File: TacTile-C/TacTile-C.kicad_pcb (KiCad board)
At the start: 2 copper layers, 59.9 x 59.9 mm, 45 parts, among them J1 Conn_01x02, J10 Conn_01x02, J11 Conn_01x02, J12 Conn_01x02, J13 Conn_01x02, J14 Conn_01x02, J15 Conn_01x02, J16 Conn_01x02, J17 Conn_01x02, J18 Conn_01x04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

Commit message: Mounted ICs without sockets to save space
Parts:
- U1: footprint Package_DIP:DIP-6_W7.62mm_Socket -> Package_DIP:DIP-6_W7.62mm
- U2, U3, U4, U5, U6, U7, U8: footprint Package_DIP:DIP-16_W7.62mm_Socket -> Package_DIP:DIP-16_W7.62mm

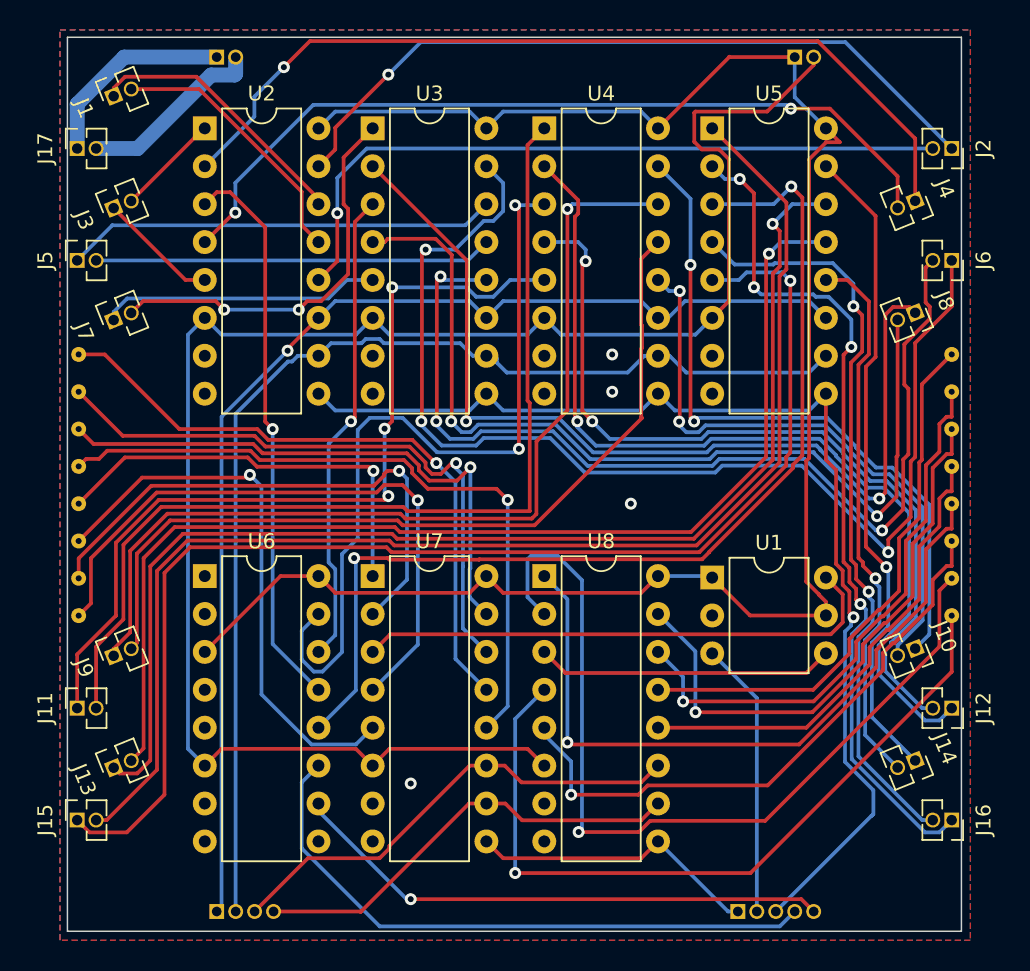
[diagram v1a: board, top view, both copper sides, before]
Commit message: Added photoresistor footprint and enlarged main boards to 60mm
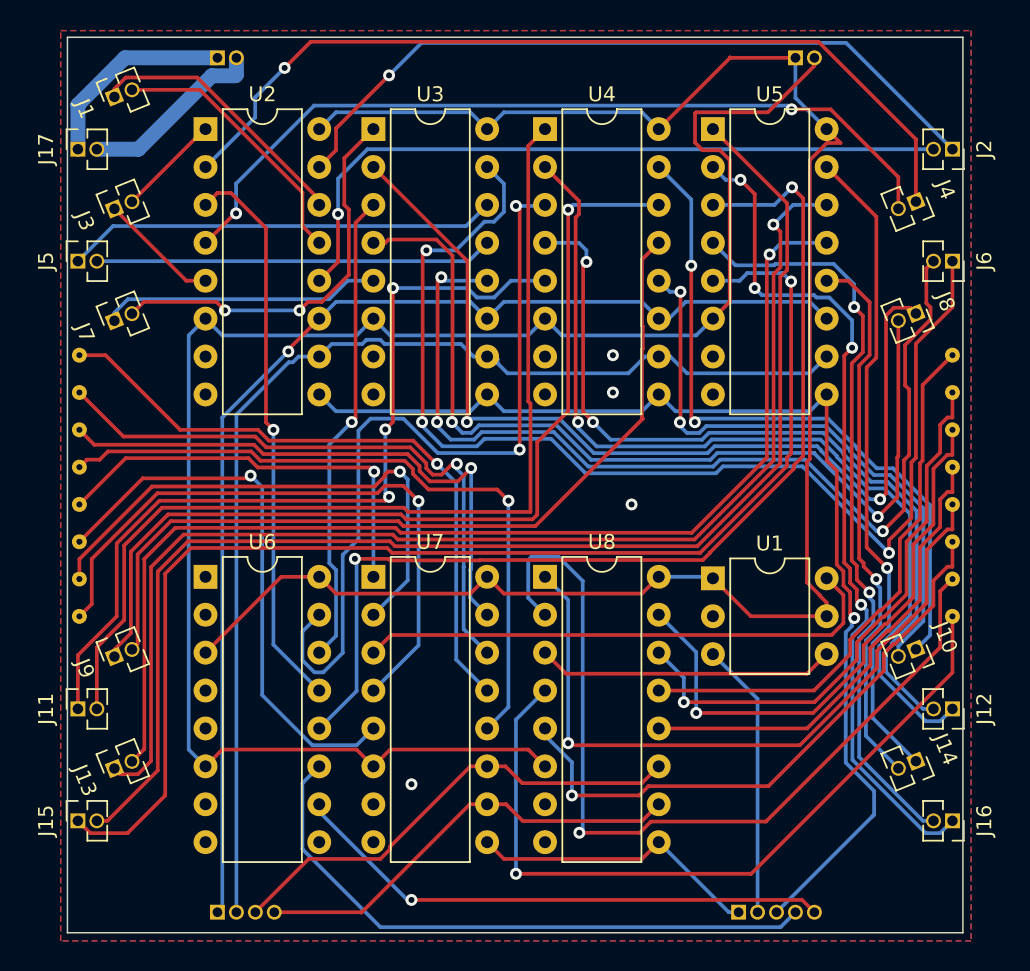
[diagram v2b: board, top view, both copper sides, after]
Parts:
- moved J4 0.07 mm to (81.9, 36.0)
- moved J8 0.07 mm to (81.9, 43.5)
- moved J1 0.07 mm to (28.1, 29.0)
- moved J11 0.07 mm to (25.7, 70.0)
- moved J13 0.07 mm to (28.1, 74.0)
- moved J15 0.07 mm to (25.7, 77.5)
- moved J17 0.07 mm to (25.7, 32.5)
- moved J20 0.07 mm to (35.0, 26.4)
- moved J21 0.07 mm to (73.8, 26.4)
- moved J3 0.07 mm to (28.1, 36.5)
- moved J5 0.07 mm to (25.7, 40.0)
- moved J7 0.07 mm to (28.1, 44.0)
- moved J9 0.07 mm to (28.1, 66.5)
- moved JMP1 0.07 mm to (25.8, 46.3)
- moved JMP2 0.07 mm to (25.8, 48.8)
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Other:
- board size 59.9 x 59.9 mm -> 60 x 60 mm

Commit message: Enlarged B-C interface to 2.54 pitch connectors
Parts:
- J18: footprint Connector_PinHeader_1.27mm:PinHeader_1x04_P1.27mm_Vertical -> Connector_PinHeader_2.54mm:PinHeader_1x04_P2.54mm_Vertical
- J19: footprint Connector_PinHeader_1.27mm:PinHeader_1x05_P1.27mm_Vertical -> Connector_PinHeader_2.54mm:PinHeader_1x05_P2.54mm_Vertical
- J20, J21: footprint Connector_PinHeader_1.27mm:PinHeader_1x02_P1.27mm_Vertical -> Connector_PinHeader_2.54mm:PinHeader_1x02_P2.54mm_Vertical
- moved J19 5.13 mm to (64.8, 83.6)
- moved J21 1.32 mm to (72.5, 26.4)
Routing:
- net /LS7: track 41.6 -> 35.9 mm
- net /LS3: track 29.7 -> 25.9 mm
- net /LS2: track 32.1 -> 29.5 mm
- net /LS4: track 19.7 -> 17.2 mm
- net /GND: track 12.5 -> 13.4 mm
- net /LS5: track 18.5 -> 17.7 mm
- net /VCC: track 123.3 -> 122.5 mm
- net /LS1: track 77.5 -> 76.8 mm
- net /LS6: track 76.0 -> 75.5 mm

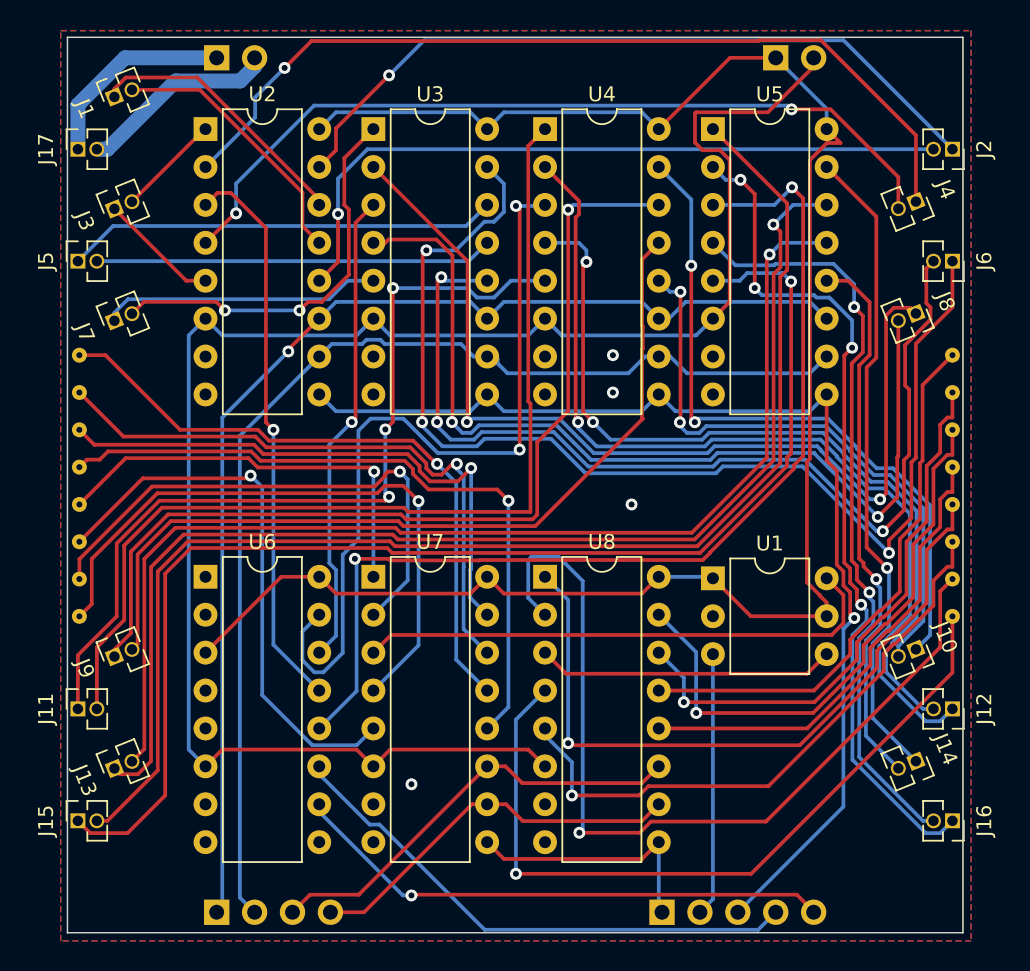
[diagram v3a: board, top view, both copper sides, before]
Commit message: Finished enlarging pins on C, D, L1, L2
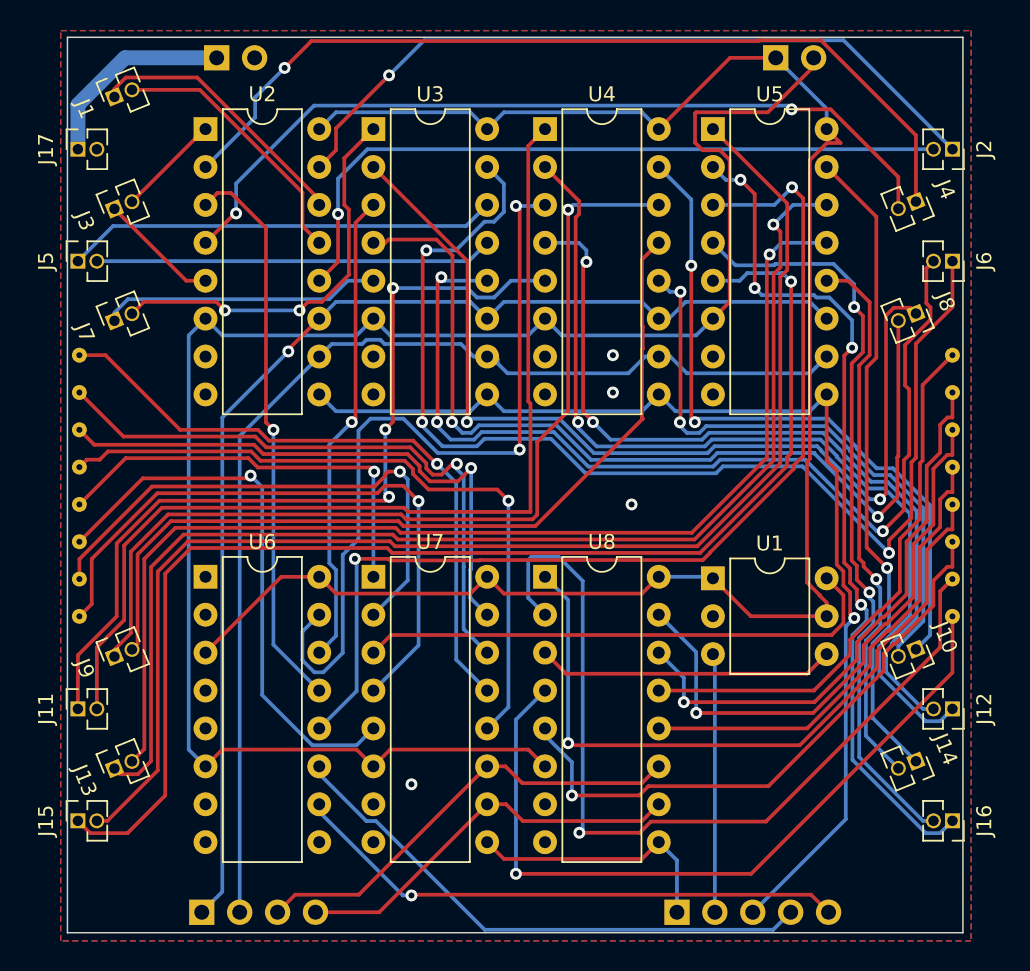
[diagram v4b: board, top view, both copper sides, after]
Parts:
- moved J18 1.00 mm to (34.0, 83.6)
- moved J19 1.00 mm to (65.8, 83.6)
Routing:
- net /GND: track 13.4 -> 0.00 mm
- net /LS3: track 25.9 -> 26.9 mm
- net /LS2: track 29.5 -> 30.5 mm
- net /LS7: track 35.9 -> 36.9 mm
- net /LS8: track 36.5 -> 37.5 mm

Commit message: Used 16DIP demultiplexer instead of single demultiplexer
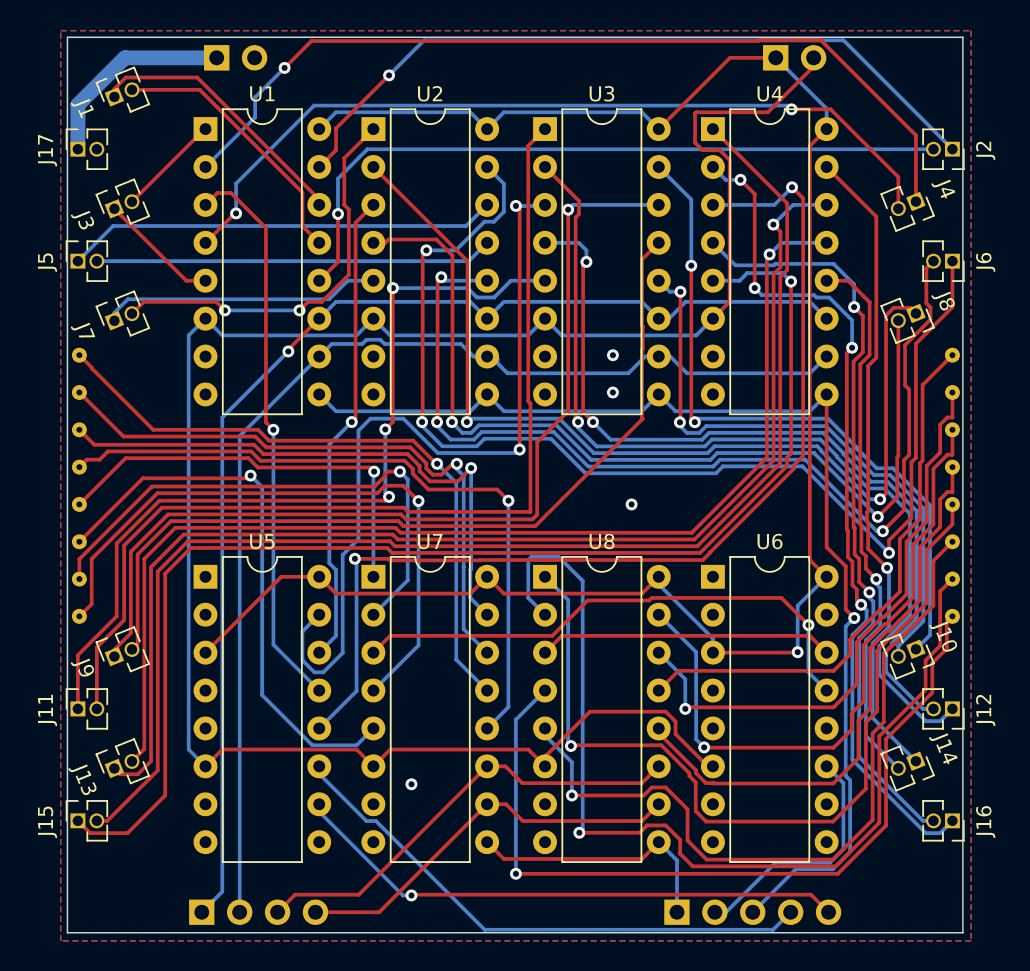
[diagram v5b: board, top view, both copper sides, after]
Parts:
- removed the U1 at (68.2, 61.2)
- added U6: 74HC4051, Package_DIP:DIP-16_W7.62mm, F.Cu at (68.2, 61.1)
- renumbered U2 to U1, U3 to U2, U4 to U3, U5 to U4, U6 to U5
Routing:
- net /LEN: track 118.0 -> 133.2 mm
- net /INP45: track 40.4 -> 50.9 mm
- net /INP44: track 48.0 -> 57.6 mm
- net /INP46: track 59.8 -> 67.1 mm
- net /INP43: track 31.8 -> 38.3 mm
- net /INP42: track 38.6 -> 43.7 mm
- net /INP47: track 51.7 -> 55.1 mm
- net /LS6: track 75.1 -> 76.8 mm
- net /INP41: track 37.6 -> 39.1 mm
- net /VCC: track 122.5 -> 123.8 mm, vias 0 -> 1
- net /LS5: track 17.3 -> 16.4 mm
- net Net-(U6-A0): track 35.8 -> 36.3 mm, vias 0 -> 1

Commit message: Redid A board with MOSFETs sinking current
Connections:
- net /INP0 renamed /B0
- net /INP1 renamed /B1
- net /INP10 renamed /B10
- net /INP11 renamed /B11
- net /INP12 renamed /B12
- net /INP13 renamed /B13
- net /INP14 renamed /B14
- net /INP15 renamed /B15
- net /INP16 renamed /B16
- net /INP17 renamed /B17
- net /INP18 renamed /B18
- net /INP19 renamed /B19
- net /INP2 renamed /B2
- net /INP20 renamed /B20
- net /INP21 renamed /B21
- net /INP22 renamed /B22
- net /INP23 renamed /B23
- net /INP24 renamed /B24
- net /INP25 renamed /B25
- net /INP26 renamed /B26
- net /INP27 renamed /B27
- net /INP28 renamed /B28
- net /INP29 renamed /B29
- net /INP3 renamed /B3
- net /INP30 renamed /B30
- net /INP31 renamed /B31
- net /INP32 renamed /A0
- net /INP33 renamed /A1
- net /INP34 renamed /A2
- net /INP35 renamed /A3
- net /INP36 renamed /A4
- net /INP37 renamed /A5
- net /INP38 renamed /A6
- net /INP39 renamed /A7
- net /INP4 renamed /B4
- net /INP40 renamed /A8
- net /INP41 renamed /A9
- net /INP42 renamed /A10
- net /INP43 renamed /A11
- net /INP44 renamed /A12
- net /INP45 renamed /A13
- net /INP46 renamed /A14
- net /INP47 renamed /A15
- net /INP5 renamed /B5
- net /INP6 renamed /B6
- net /INP7 renamed /B7
- net /INP8 renamed /B8
- net /INP9 renamed /B9

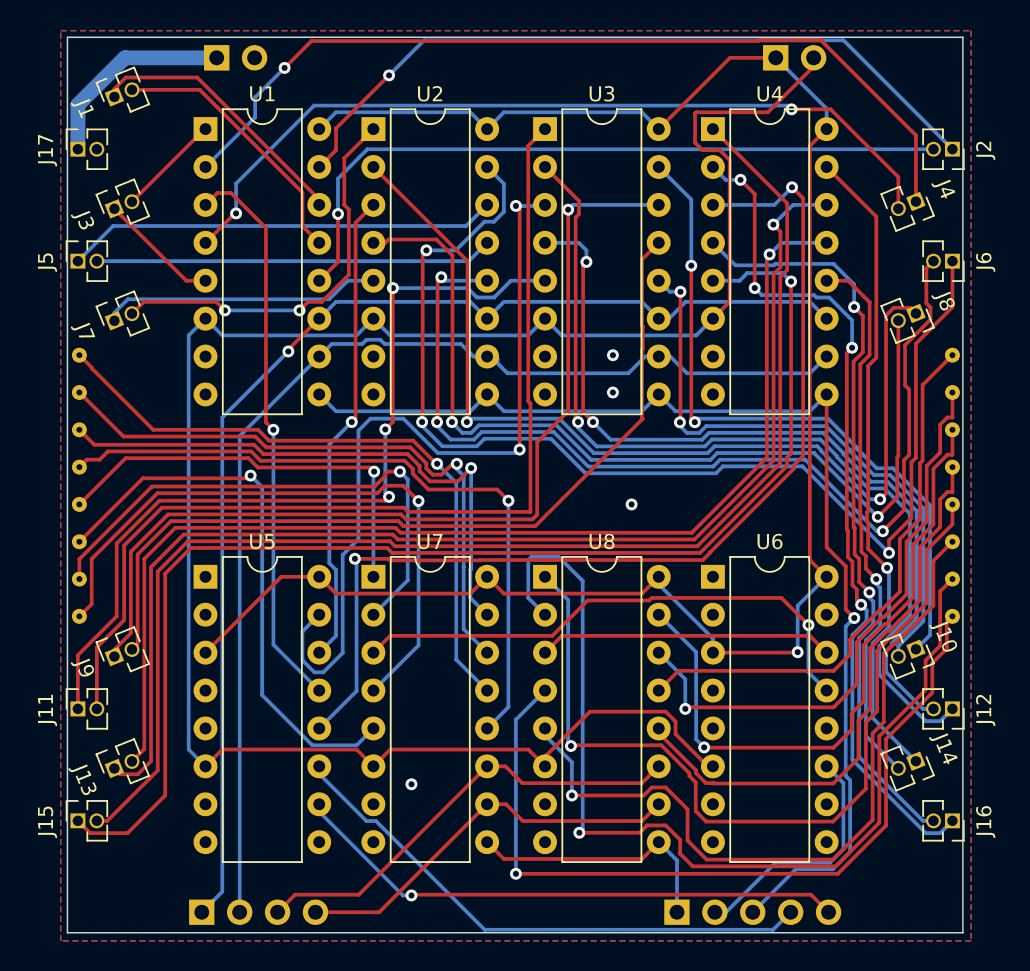
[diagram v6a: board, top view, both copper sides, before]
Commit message: Added voltage input to A MOSFETs
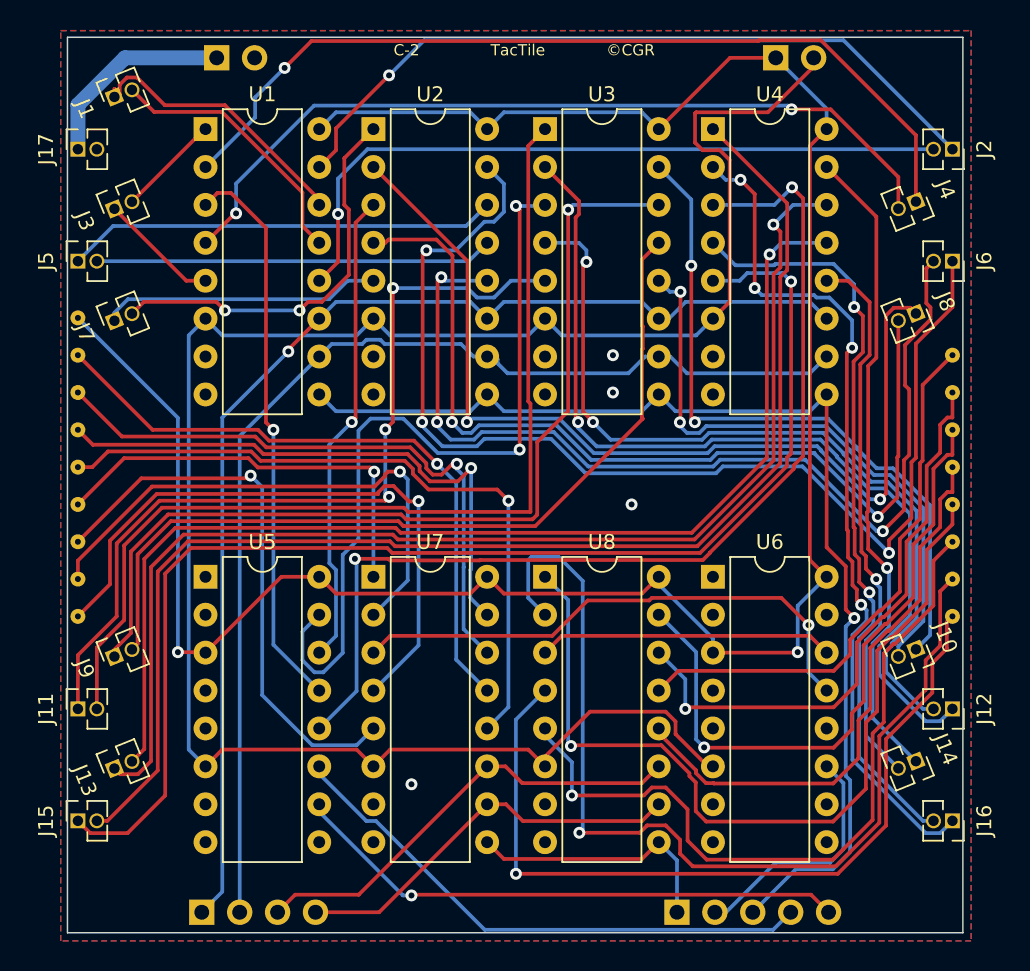
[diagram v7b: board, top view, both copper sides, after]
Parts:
- added JMP17: ~, TacTile:Jumper_Connect, F.Cu at (25.7, 43.8)
- moved JMP1 0.10 mm to (25.7, 46.3)
- moved JMP2 0.10 mm to (25.7, 48.8)
- moved JMP3 0.10 mm to (25.7, 51.3)
- moved JMP4 0.10 mm to (25.7, 53.8)
- moved JMP5 0.10 mm to (25.7, 56.3)
- moved JMP6 0.10 mm to (25.7, 58.8)
- moved JMP7 0.10 mm to (25.7, 61.3)
- moved JMP8 0.10 mm to (25.7, 63.8)
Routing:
- net /VCC: track 123.8 -> 150.8 mm, vias 1 -> 2
- net /B1: track 18.3 -> 19.0 mm
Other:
- board text added: "C-2"
- board text added: "TacTile"
- board text added: "©CGR"
